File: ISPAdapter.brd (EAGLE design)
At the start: 76 x 38 mm, 9 parts, among them U1 SWITCH_IC_QUAD74LVC4066

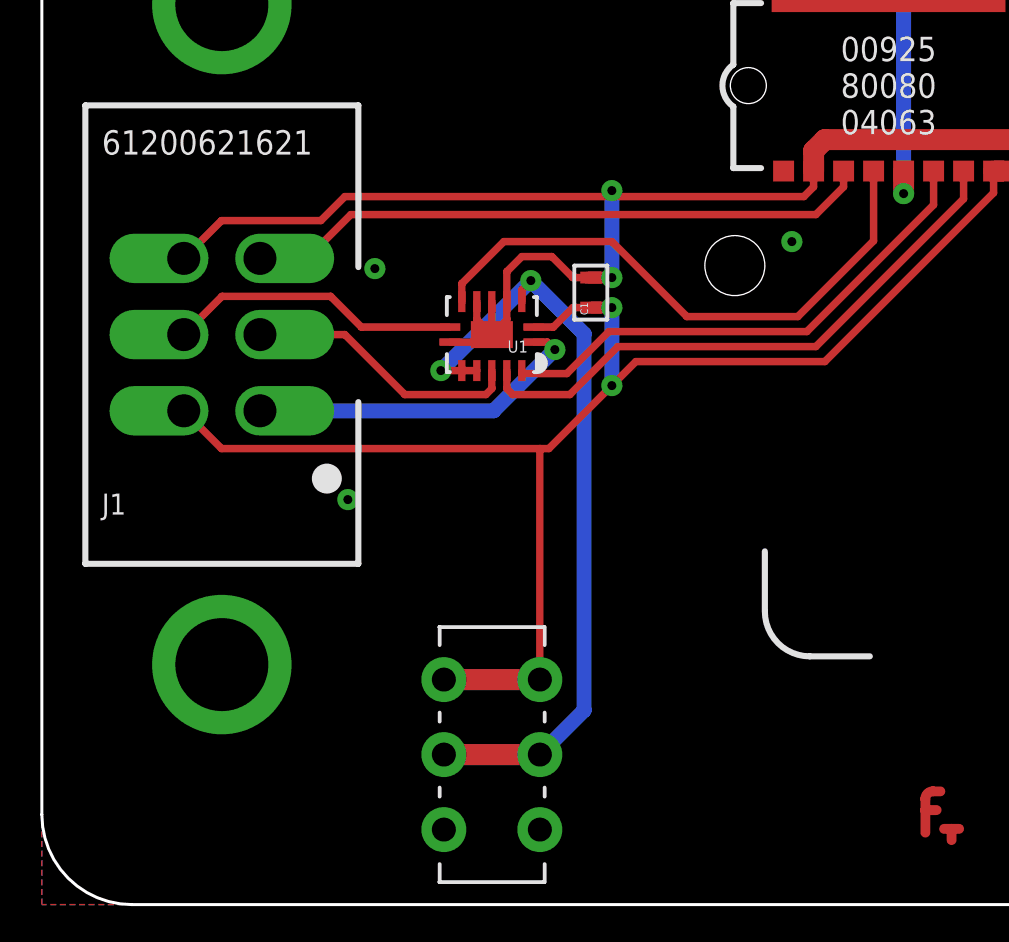
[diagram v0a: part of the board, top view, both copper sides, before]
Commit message: Switch IC fitting
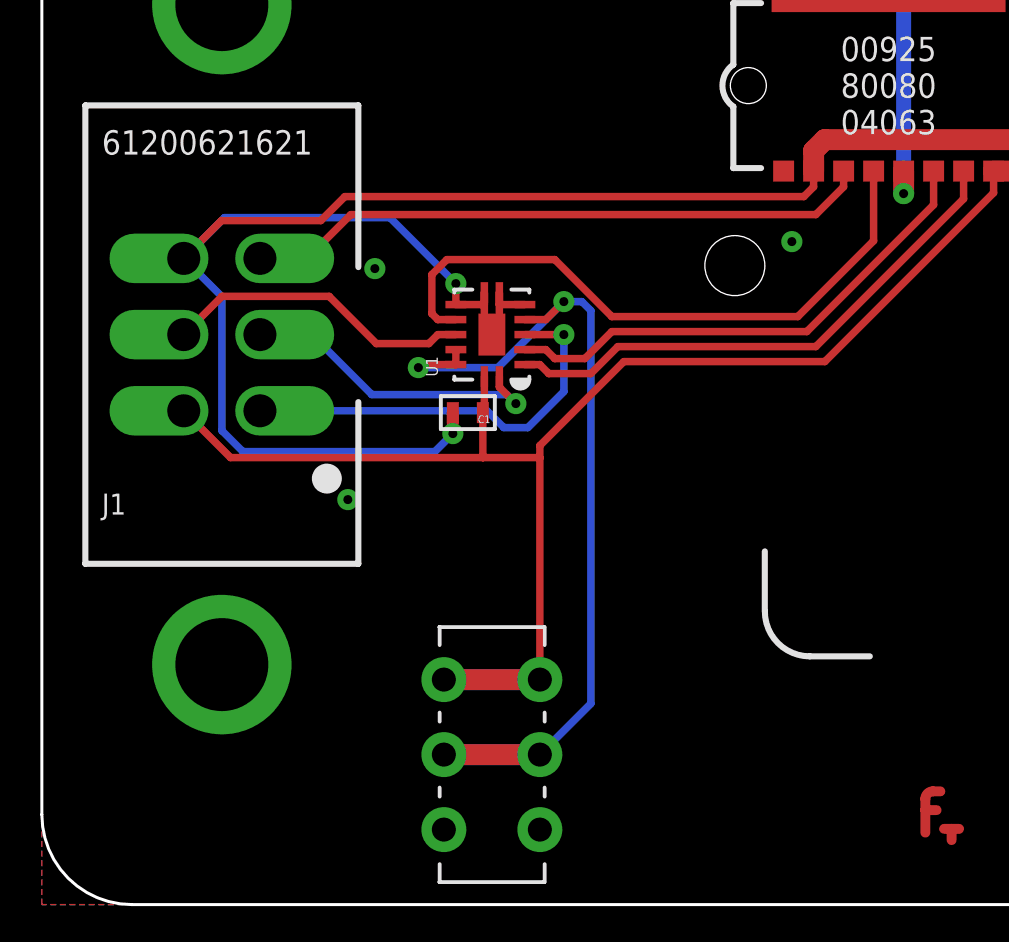
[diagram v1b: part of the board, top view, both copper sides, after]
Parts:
- moved C1 5.73 mm to (14.2, 16.4), turned to 180 degrees
- turned U1 to 90 degrees
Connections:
- net DGND: now also U1.6, U1.8, U1.9; no longer U1.10, U1.11, U1.12
- net ISP_EN: now also U1.12; no longer U1.6
- net MISO: now also U1.3; no longer U1.2
- net MISO_A: now also U1.4; no longer U1.1
- net MOSI: now also U1.10; no longer U1.9
- net MOSI_A: now also U1.11; no longer U1.8
- net SCK: now also U1.2; no longer U1.3
- net SCK_A: now also U1.1; no longer U1.4
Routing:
- net DGND: track 58.5 -> 77.0 mm
- net MISO_A: track 11.5 -> 14.1 mm
- net VCC: track 69.3 -> 66.8 mm, vias 2 -> 0
- net ISP_EN: track 29.8 -> 32.0 mm
- net MOSI: track 19.3 -> 21.3 mm
- net SCK: track 19.5 -> 18.1 mm
- net SCK_A: track 9.24 -> 10.6 mm, vias 0 -> 1
- net MOSI_A: track 9.82 -> 10.4 mm

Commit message: Tidy
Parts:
- moved C1 0.81 mm to (15.0, 16.3), turned to 0 degrees
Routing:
- net DGND: track 77.0 -> 78.8 mm
- net ISP_EN: track 32.0 -> 31.0 mm
- net MISO_A: track 14.1 -> 13.5 mm
- net SCK_A: track 10.6 -> 11.2 mm
- net GND: vias 8 -> 7

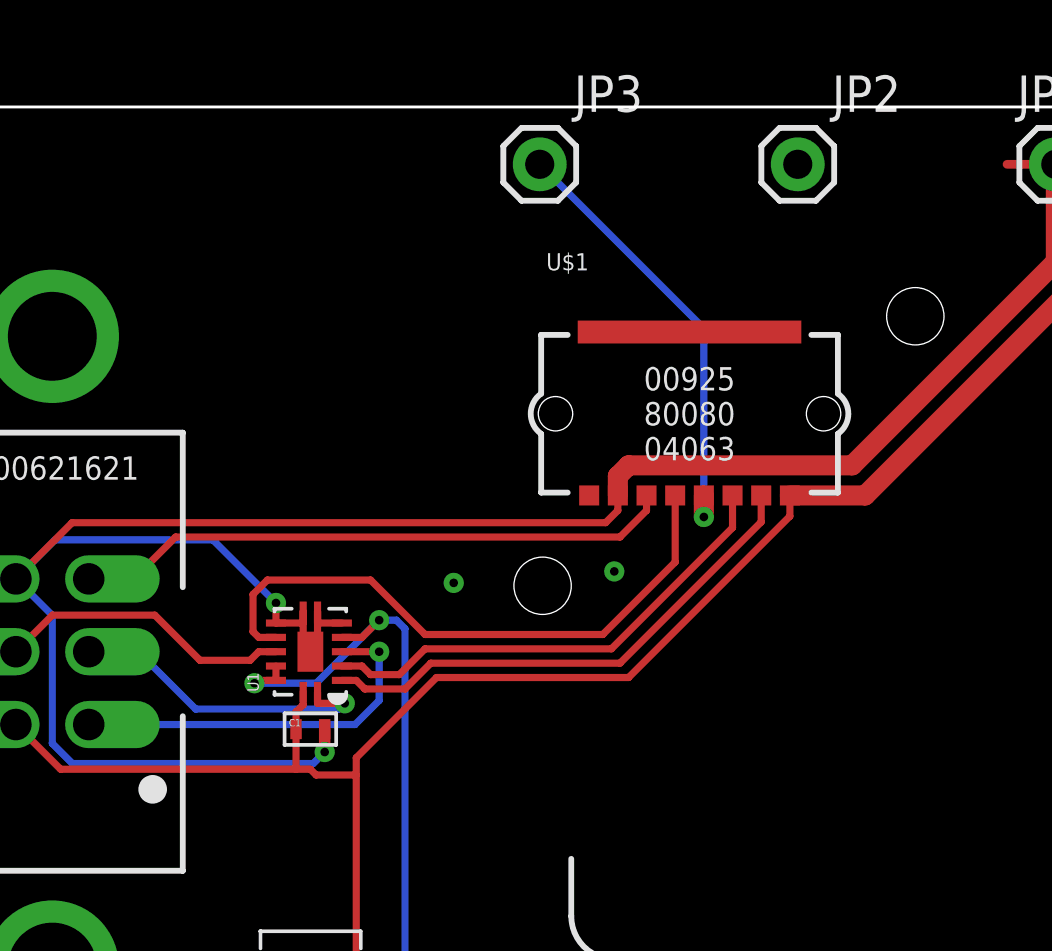
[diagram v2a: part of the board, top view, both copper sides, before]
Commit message: Full connector mapping
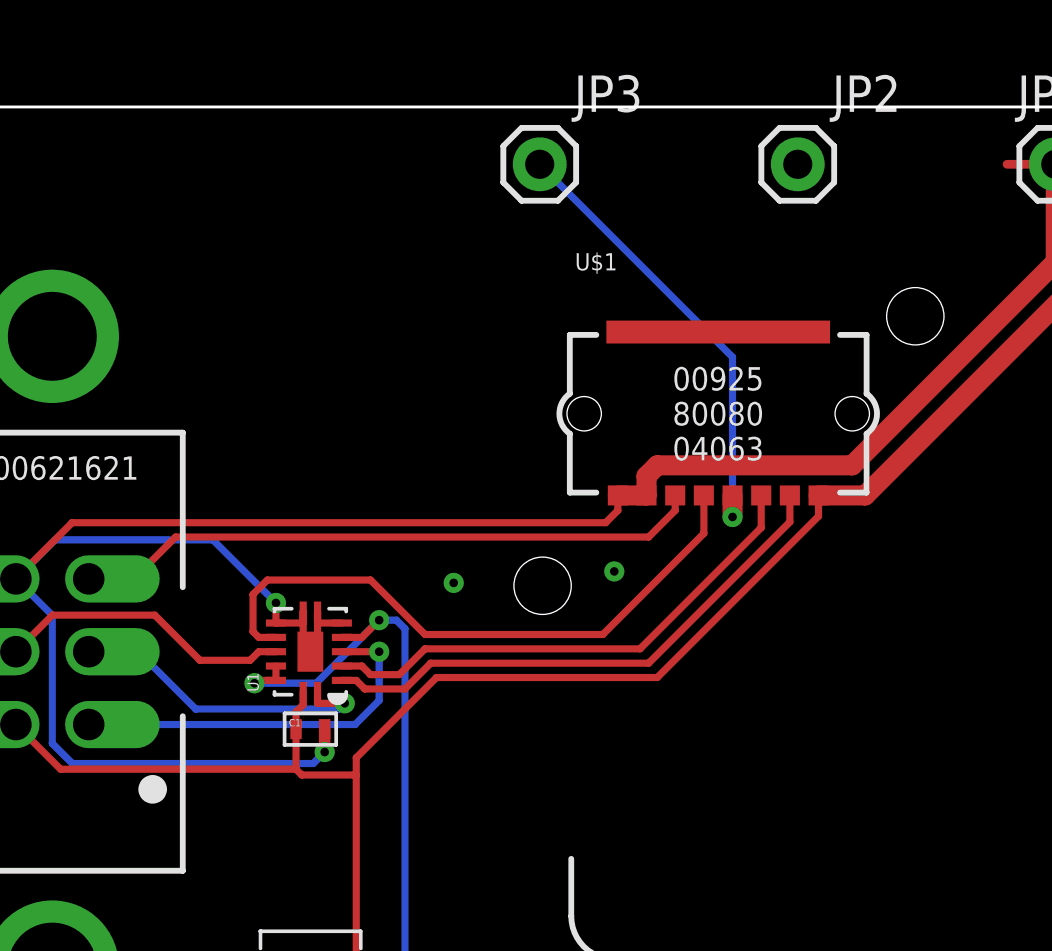
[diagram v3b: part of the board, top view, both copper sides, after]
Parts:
- moved U$1 1.00 mm to (29.2, 27.3)
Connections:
- net DGND: now also U$1.8
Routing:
- net SCK: track 18.1 -> 19.1 mm
- net RESET: track 21.0 -> 22.0 mm
- net MISO: track 17.0 -> 18.0 mm
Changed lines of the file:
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@@
 <wire x1="26.1" y1="10.3" x2="26.1" y2="17.3" width="0.2032" layer="107"/>
 <wire x1="33.1" y1="17.3" x2="33.1" y2="10.3" width="0.2032" layer="107"/>
-<text x="29.7" y="23.7" size="0.8128" layer="107" font="vector" ratio="15" align="top-center">1</text>
-<text x="31.7" y="23.7" size="0.8128" layer="107" font="vector" ratio="15" align="top-center">2</text>
-<text x="30.7" y="23.7" size="0.8128" layer="107" font="vector" ratio="15" align="top-center">3</text>
-<text x="27.7" y="23.7" size="0.8128" layer="107" font="vector" ratio="15" align="top-center">4</text>
-<text x="26.7" y="23.7" size="0.8128" layer="107" font="vector" ratio="15" align="top-center">5</text>
-<text x="25.7" y="23.7" size="0.8128" layer="107" font="vector" ratio="15" align="top-center">6</text>
+<text x="30.8" y="23.7" size="0.8128" layer="107" font="vector" ratio="15" align="top-center">1</text>
+<text x="32.8" y="23.7" size="0.8128" layer="107" font="vector" ratio="15" align="top-center">2</text>
+<text x="31.8" y="23.7" size="0.8128" layer="107" font="vector" ratio="15" align="top-center">3</text>
+<text x="28.8" y="23.7" size="0.8128" layer="107" font="vector" ratio="15" align="top-center">4</text>
+<text x="27.8" y="23.7" size="0.8128" layer="107" font="vector" ratio="15" align="top-center">5</text>
+<text x="26.8" y="23.7" size="0.8128" layer="107" font="vector" ratio="15" align="top-center">6</text>
 <circle x="36.1" y="30.7" radius="1.7" width="0.5" layer="107"/>
 <hole x="44.1" y="11.9" drill="2"/>
@@
 <text x="18" y="0.7" size="1.5" layer="107" font="vector" ratio="15">DW</text>
 <text x="18" y="9.3" size="1.5" layer="107" font="vector" ratio="15" align="top-left">SPI</text>
+<text x="25.8" y="23.7" size="0.8128" layer="107" font="vector" ratio="15" align="top-center">6</text>
 </plain>
 <attributes>
@@
 </element>
 <element name="JP1" library="SparkFun-Connectors" package="1X02" value="M02PTH" x="41" y="36"/>
-<element name="U$1" library="dubec" package="AVX9258-8C" value="AVX9258" x="28.225" y="27.3">
-<attribute name="MANUFACTURER" value="AVX Corporation" x="28.225" y="27.3" size="1.778" layer="27" display="off"/>
-<attribute name="EURO" value="1.30" x="28.225" y="27.3" size="1.778" layer="27" display="off"/>
-<attribute name="MFG_PART_#" value="009258008004063" x="28.225" y="27.3" size="1.778" layer="27" display="off"/>
-<attribute name="DIGIKEY_PART_#" value="478-5495-1-ND" x="28.225" y="27.3" size="1.778" layer="27" display="off"/>
+<element name="U$1" library="dubec" package="AVX9258-8C" value="AVX9258" x="29.225" y="27.3">
+<attribute name="MANUFACTURER" value="AVX Corporation" x="29.225" y="27.3" size="1.778" layer="27" display="off"/>
+<attribute name="EURO" value="1.30" x="29.225" y="27.3" size="1.778" layer="27" display="off"/>
+<attribute name="MFG_PART_#" value="009258008004063" x="29.225" y="27.3" size="1.778" layer="27" display="off"/>
+<attribute name="DIGIKEY_PART_#" value="478-5495-1-ND" x="29.225" y="27.3" size="1.778" layer="27" display="off"/>
 </element>
 <element name="JP2" library="SparkFun-Connectors" package="1X01" value="M01PTH" x="32" y="36"/>
@@
 <contactref element="U$1" pad="1"/>
 <contactref element="U1" pad="14"/>
-<wire x1="31.725" y1="24.45" x2="34.35" y2="24.45" width="0.7" layer="1"/>
+<wire x1="32.725" y1="24.45" x2="34.35" y2="24.45" width="0.7" layer="1"/>
 <wire x1="34.35" y1="24.45" x2="43.54" y2="33.64" width="0.7" layer="1"/>
 <wire x1="43.54" y1="33.64" x2="43.54" y2="36" width="0.7" layer="1"/>
-<wire x1="31.725" y1="23.725" x2="26.1" y2="18.1" width="0.25" layer="1"/>
-<wire x1="26.1" y1="18.1" x2="19.4" y2="18.1" width="0.25" layer="1"/>
+<wire x1="32.725" y1="23.725" x2="27.1" y2="18.1" width="0.25" layer="1"/>
+<wire x1="27.1" y1="18.1" x2="19.4" y2="18.1" width="0.25" layer="1"/>
 <contactref element="S1" pad="1"/>
 <contactref element="S1" pad="4"/>
 <wire x1="13.4" y1="7.5" x2="16.6" y2="7.5" width="0.7" layer="16"/>
 <wire x1="13.4" y1="7.5" x2="16.6" y2="7.5" width="0.7" layer="1"/>
-<wire x1="31.725" y1="23.725" x2="31.725" y2="24.45" width="0.25" layer="1"/>
+<wire x1="32.725" y1="23.725" x2="32.725" y2="24.45" width="0.25" layer="1"/>
 <wire x1="4.73" y1="16.46" x2="6.29" y2="14.9" width="0.25" layer="1"/>
 <wire x1="6.29" y1="14.9" x2="14.5" y2="14.9" width="0.25" layer="1"/>
-<wire x1="14.5" y1="14.9" x2="15" y2="14.9" width="0.25" layer="1"/>
-<wire x1="15" y1="14.9" x2="15.2" y2="14.7" width="0.25" layer="1"/>
-<wire x1="15.2" y1="14.7" x2="16.6" y2="14.7" width="0.25" layer="1"/>
+<wire x1="14.5" y1="14.9" x2="14.7" y2="14.7" width="0.25" layer="1"/>
+<wire x1="14.7" y1="14.7" x2="16.6" y2="14.7" width="0.25" layer="1"/>
 <wire x1="16.6" y1="7.5" x2="16.6" y2="14.7" width="0.25" layer="1"/>
 <contactref element="C1" pad="1"/>
@@
 <signal name="MOSI">
 <contactref element="U$1" pad="5"/>
-<wire x1="27.725" y1="24.45" x2="27.725" y2="22.125" width="0.25" layer="1"/>
-<wire x1="27.725" y1="22.125" x2="25.2" y2="19.6" width="0.25" layer="1"/>
+<wire x1="28.725" y1="24.45" x2="28.725" y2="23.125" width="0.25" layer="1"/>
+<wire x1="28.725" y1="23.125" x2="25.2" y2="19.6" width="0.25" layer="1"/>
 <contactref element="U1" pad="10"/>
 <wire x1="25.2" y1="19.6" x2="19" y2="19.6" width="0.25" layer="1"/>
@@
 <contactref element="J1" pad="6"/>
 <contactref element="JP1" pad="1"/>
-<wire x1="26.1" y1="25.5" x2="25.725" y2="25.125" width="0.7" layer="1"/>
+<wire x1="27.1" y1="25.5" x2="26.725" y2="25.125" width="0.7" layer="1"/>
 <contactref element="U$1" pad="7"/>
-<wire x1="26.1" y1="25.5" x2="33.9" y2="25.5" width="0.7" layer="1"/>
+<wire x1="27.1" y1="25.5" x2="33.9" y2="25.5" width="0.7" layer="1"/>
 <wire x1="33.9" y1="25.5" x2="41" y2="32.6" width="0.7" layer="1"/>
 <wire x1="41" y1="32.6" x2="41" y2="36" width="0.7" layer="1"/>
@@
 <wire x1="25.3" y1="23.5" x2="6.69" y2="23.5" width="0.25" layer="1"/>
 <wire x1="6.69" y1="23.5" x2="4.73" y2="21.54" width="0.25" layer="1"/>
-<wire x1="25.725" y1="23.925" x2="25.725" y2="24.45" width="0.25" layer="1"/>
-<wire x1="25.725" y1="25.125" x2="25.725" y2="24.45" width="0.7" layer="1"/>
+<wire x1="26.725" y1="25.125" x2="26.725" y2="24.45" width="0.7" layer="1"/>
 <contactref element="U1" pad="7"/>
 <contactref element="U1" pad="PAD"/>
@@
 <wire x1="11.6" y1="22.9" x2="6.09" y2="22.9" width="0.25" layer="16"/>
 <wire x1="6.09" y1="22.9" x2="4.73" y2="21.54" width="0.25" layer="16"/>
+<contactref element="U$1" pad="8"/>
+<wire x1="25.725" y1="23.925" x2="25.725" y2="24.45" width="0.25" layer="1"/>
+<wire x1="26.725" y1="24.45" x2="25.725" y2="24.45" width="0.7" layer="1"/>
 </signal>
 <signal name="MISO">
 <contactref element="U$1" pad="3"/>
-<wire x1="29.725" y1="23.325" x2="25.5" y2="19.1" width="0.25" layer="1"/>
-<wire x1="25.5" y1="19.1" x2="19" y2="19.1" width="0.25" layer="1"/>
-<wire x1="29.725" y1="23.325" x2="29.725" y2="24.45" width="0.25" layer="1"/>
+<wire x1="30.725" y1="23.325" x2="26.5" y2="19.1" width="0.25" layer="1"/>
+<wire x1="26.5" y1="19.1" x2="19" y2="19.1" width="0.25" layer="1"/>
+<wire x1="30.725" y1="23.325" x2="30.725" y2="24.45" width="0.25" layer="1"/>
 <contactref element="U1" pad="3"/>
 <wire x1="19" y1="19.1" x2="18.1" y2="18.2" width="0.25" layer="1"/>
@@
 <signal name="SCK">
 <contactref element="U$1" pad="2"/>
-<wire x1="30.725" y1="23.525" x2="25.8" y2="18.6" width="0.25" layer="1"/>
-<wire x1="25.8" y1="18.6" x2="19.2" y2="18.6" width="0.25" layer="1"/>
-<wire x1="30.725" y1="23.525" x2="30.725" y2="24.45" width="0.25" layer="1"/>
+<wire x1="31.725" y1="23.525" x2="26.8" y2="18.6" width="0.25" layer="1"/>
+<wire x1="26.8" y1="18.6" x2="19.2" y2="18.6" width="0.25" layer="1"/>
+<wire x1="31.725" y1="23.525" x2="31.725" y2="24.45" width="0.25" layer="1"/>
 <contactref element="U1" pad="2"/>
 <wire x1="19.2" y1="18.6" x2="18.3" y2="17.7" width="0.25" layer="1"/>
@@
 <contactref element="J1" pad="5"/>
 <contactref element="U$1" pad="6"/>
-<wire x1="26.725" y1="23.925" x2="25.8" y2="23" width="0.25" layer="1"/>
-<wire x1="25.8" y1="23" x2="10.3" y2="23" width="0.25" layer="1"/>
+<wire x1="27.725" y1="23.925" x2="26.8" y2="23" width="0.25" layer="1"/>
+<wire x1="26.8" y1="23" x2="10.3" y2="23" width="0.25" layer="1"/>
 <wire x1="10.3" y1="23" x2="8.84" y2="21.54" width="0.25" layer="1"/>
 <wire x1="8.84" y1="21.54" x2="7.27" y2="21.54" width="0.25" layer="1"/>
-<wire x1="26.725" y1="23.925" x2="26.725" y2="24.45" width="0.25" layer="1"/>
+<wire x1="27.725" y1="23.925" x2="27.725" y2="24.45" width="0.25" layer="1"/>
 </signal>
 <signal name="GND">
@@
 <contactref element="U$1" pad="4"/>
 <contactref element="JP3" pad="1"/>
-<via x="28.725" y="23.7" extent="1-16" drill="0.3"/>
-<wire x1="28.725" y1="24.45" x2="28.725" y2="23.7" width="0.7" layer="1"/>
-<wire x1="28.725" y1="30.275" x2="23" y2="36" width="0.25" layer="16"/>
-<wire x1="28.725" y1="23.7" x2="28.725" y2="30.275" width="0.25" layer="16"/>
+<via x="29.725" y="23.7" extent="1-16" drill="0.3"/>
+<wire x1="29.725" y1="24.45" x2="29.725" y2="23.7" width="0.7" layer="1"/>
+<wire x1="29.725" y1="29.275" x2="23" y2="36" width="0.25" layer="16"/>
+<wire x1="29.725" y1="29.275" x2="29.725" y2="23.7" width="0.25" layer="16"/>
 </signal>
 <signal name="ISP_EN">
